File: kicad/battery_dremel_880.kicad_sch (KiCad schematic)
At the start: 6 parts

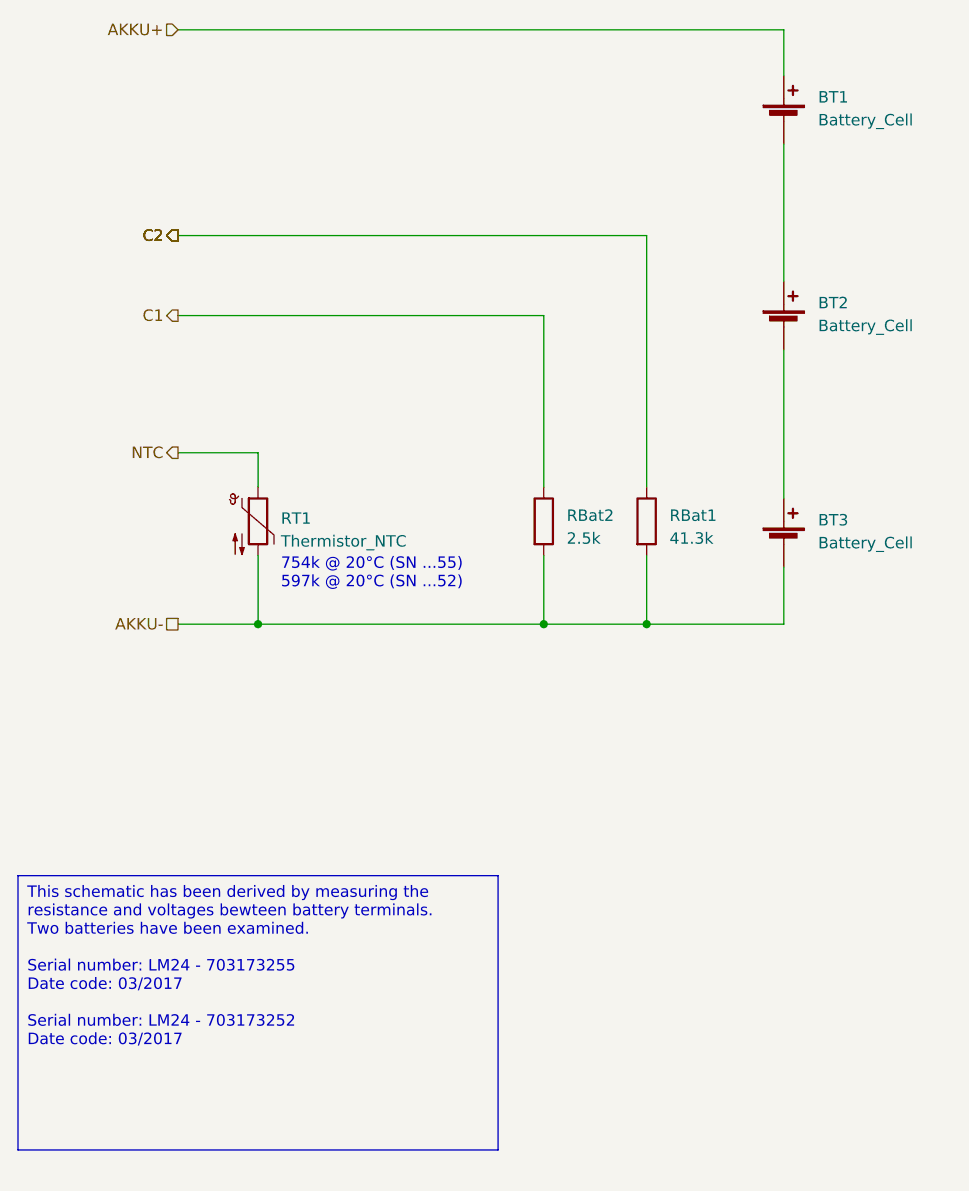
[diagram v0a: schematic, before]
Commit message: Adds dremel battery schematic
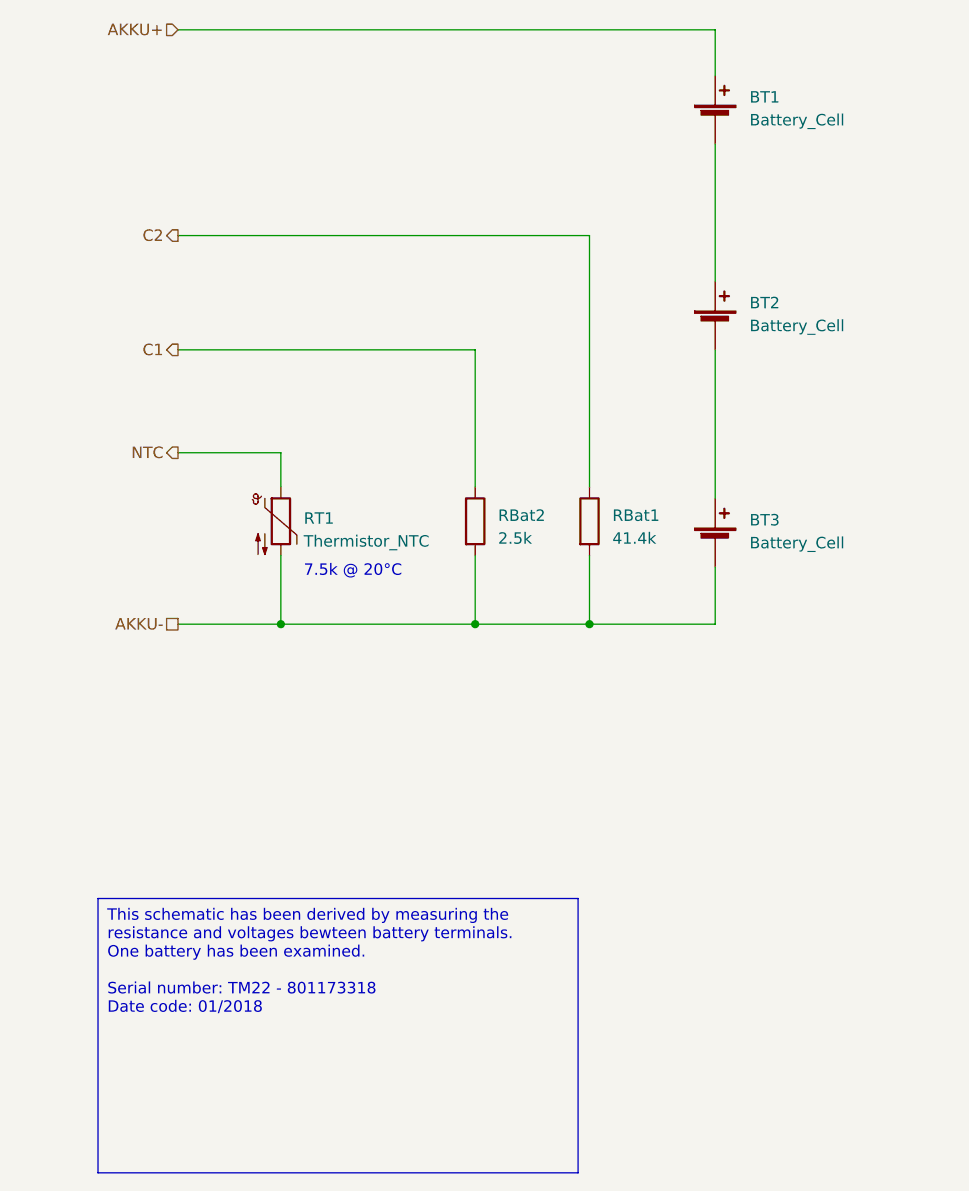
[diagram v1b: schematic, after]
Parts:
- RBat1: value 41.3k -> 41.4k
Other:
- note added: "7.5k @ 20°C"
- note removed: "754k @ 20°C (SN ...55) 597k @ 20°C (SN ...52)"
- company: Robert Bosch Power Tools GmbH -> Dremel
